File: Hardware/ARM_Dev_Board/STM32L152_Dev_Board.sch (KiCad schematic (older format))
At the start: 21 parts, among them J1 SWD_Header, J2 Conn_01x20_Female, J3 Conn_01x22_Female, J4 Eurorack_10_pin_power, SW1 SW_Push, U1 STM32L451CCUx, U4 LM1117-3.3, Y1 Crystal

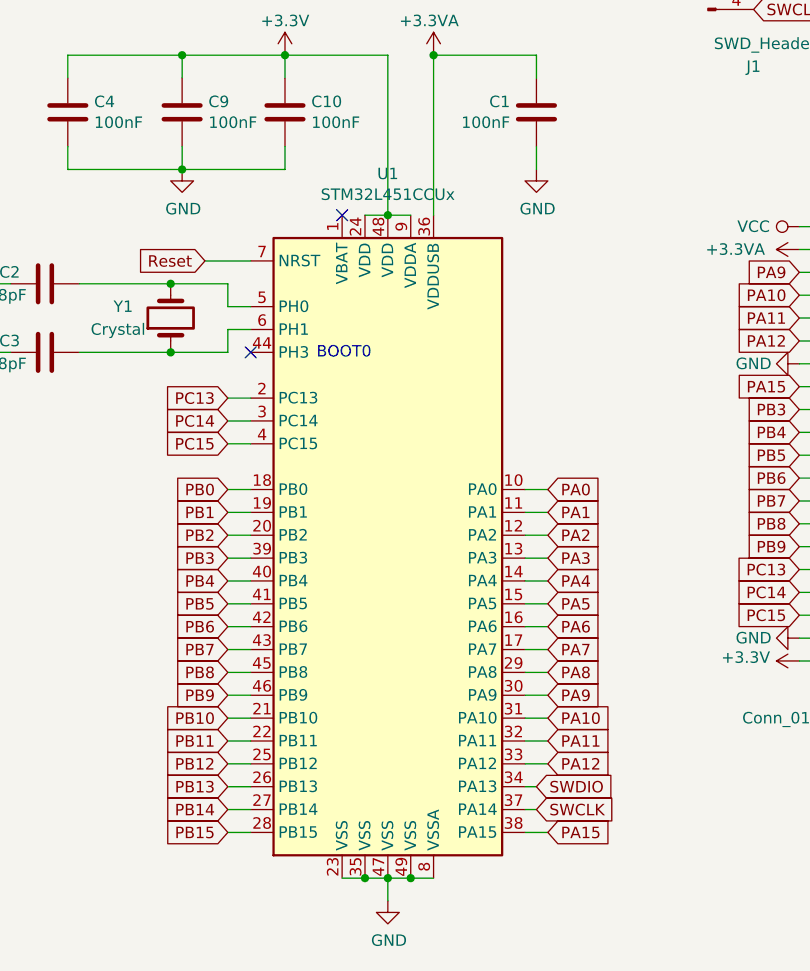
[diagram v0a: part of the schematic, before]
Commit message: Dev Board 1.1 layout finalised and gerbers sent to manufacturing
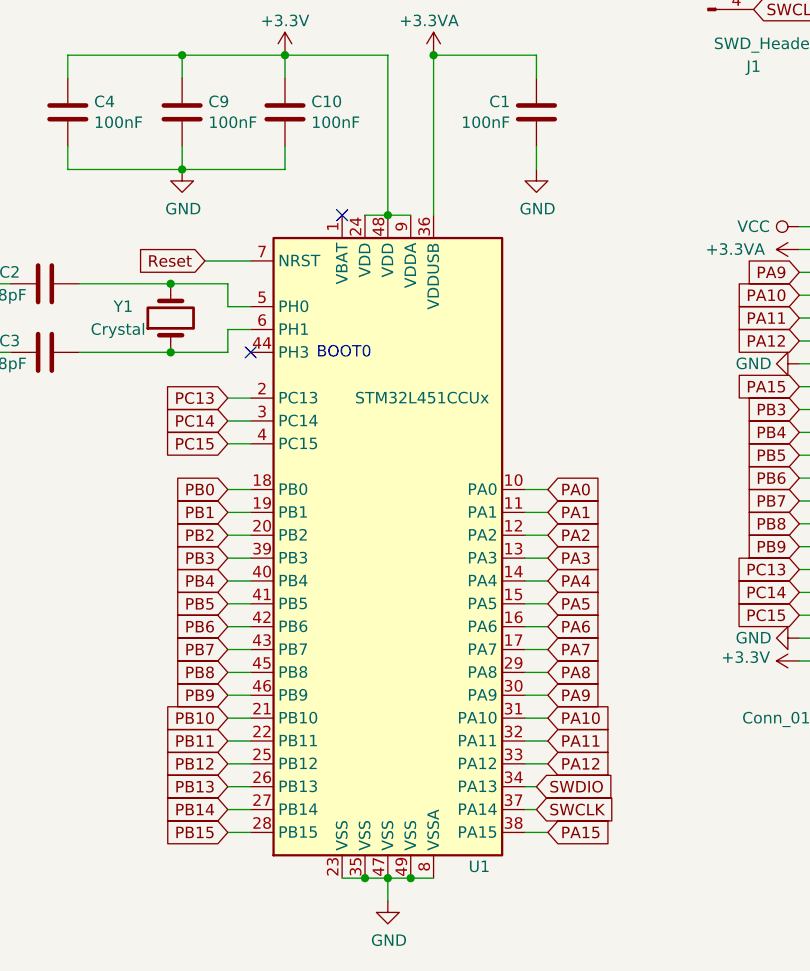
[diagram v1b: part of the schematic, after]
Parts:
- U4: footprint TO_SOT_Packages_SMD:TO-252-3_TabPin2 -> TO_SOT_Packages_SMD:SOT-223
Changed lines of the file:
@@
 F 0 "U4" H 7600 3892 50  0000 C CNN
 F 1 "LM1117-3.3" H 7600 3801 50  0000 C CNN
-F 2 "TO_SOT_Packages_SMD:TO-252-3_TabPin2" H 7600 3650 50  0001 C CNN
+F 2 "TO_SOT_Packages_SMD:SOT-223" H 7600 3650 50  0001 C CNN
 F 3 "http://www.ti.com/lit/ds/symlink/lm1117.pdf" H 7600 3650 50  0001 C CNN
 	1    7600 3650
@@
 U 1 1 5E448758
 P 2550 3750
-F 0 "U1" H 2550 5331 50  0000 C CNN
-F 1 "STM32L451CCUx" H 2550 5240 50  0000 C CNN
+F 0 "U1" H 2950 2300 50  0000 C CNN
+F 1 "STM32L451CCUx" H 2700 4350 50  0000 C CNN
 F 2 "Custom_Footprints:ARM-UQFN-48-7x7mm_Pitch0.5mm" H 2050 2350 50  0001 R CNN
 F 3 "http://www.st.com/st-web-ui/static/active/en/resource/technical/document/datasheet/DM00340475.pdf" H 2550 3750 50  0001 C CNN
@@
 $EndComp
 $Comp
-L power:+3.3VA #PWR?
+L power:+3.3VA #PWR0113
 U 1 1 5E98768A
 P 4350 2500
-F 0 "#PWR?" H 4350 2350 50  0001 C CNN
+F 0 "#PWR0113" H 4350 2350 50  0001 C CNN
 F 1 "+3.3VA" V 4350 2650 50  0000 L CNN
 F 2 "" H 4350 2500 50  0001 C CNN

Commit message: Added early draft of support for ICE40UP5k FPGA
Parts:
- C22, C23: footprint Capacitors_SMD:CP_Elec_4x5.8 -> Custom_Footprints:CP_Elec_4x5.8_Big_pad
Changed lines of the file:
@@
 F 0 "C22" V 7395 1450 50  0000 C CNN
 F 1 "22uF" V 7486 1450 50  0000 C CNN
-F 2 "Capacitors_SMD:CP_Elec_4x5.8" H 7688 1300 50  0001 C CNN
+F 2 "Custom_Footprints:CP_Elec_4x5.8_Big_pad" H 7688 1300 50  0001 C CNN
 F 3 "~" H 7650 1450 50  0001 C CNN
 	1    7650 1450
@@
 F 0 "C23" V 7905 2800 50  0000 C CNN
 F 1 "22uF" V 7814 2800 50  0000 C CNN
-F 2 "Capacitors_SMD:CP_Elec_4x5.8" H 7688 2650 50  0001 C CNN
+F 2 "Custom_Footprints:CP_Elec_4x5.8_Big_pad" H 7688 2650 50  0001 C CNN
 F 3 "~" H 7650 2800 50  0001 C CNN
 	1    7650 2800

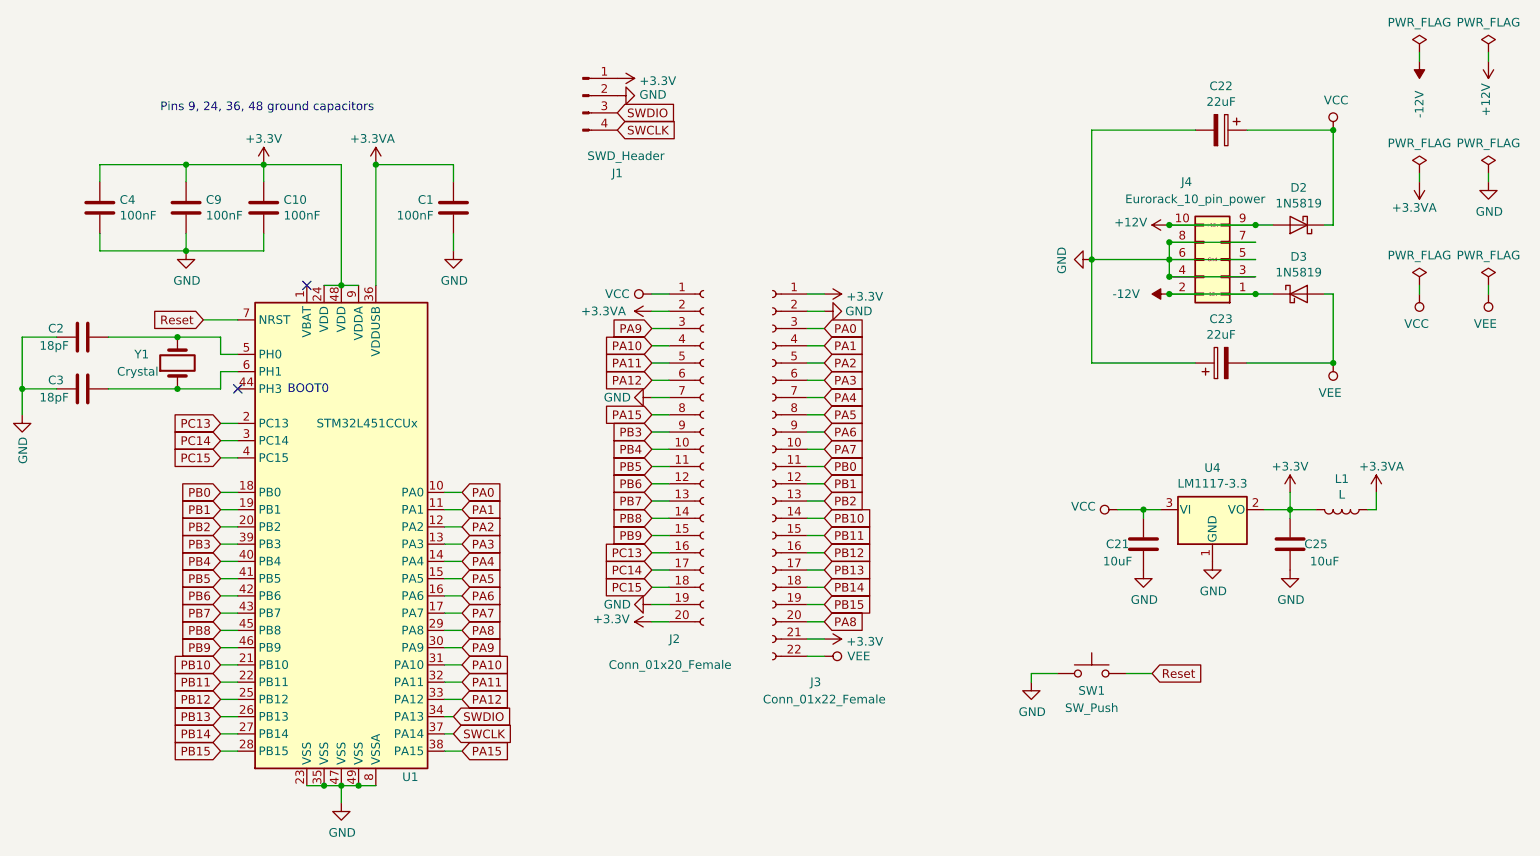
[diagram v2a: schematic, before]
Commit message: Rev 2 of dev board; provisional handling for overflow on output samples
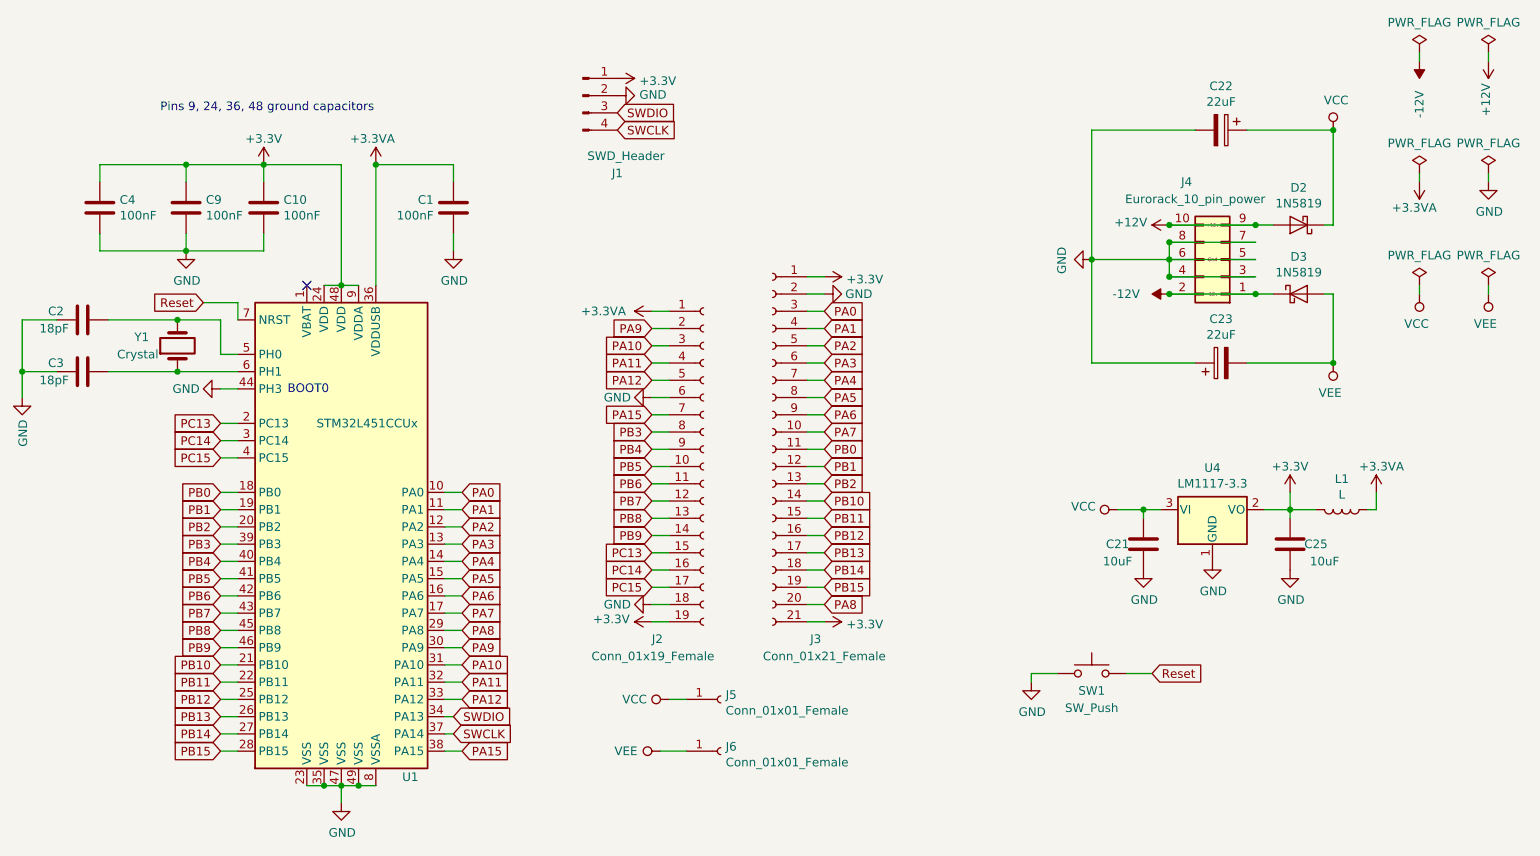
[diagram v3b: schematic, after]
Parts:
- removed J2: Conn_01x20_Female, Pin_Headers:Pin_Header_Straight_1x20_Pitch2.54mm, symbol Connector:Conn_01x20_Female
- removed J3: Conn_01x22_Female, Pin_Headers:Pin_Header_Straight_1x22_Pitch2.54mm, symbol Connector:Conn_01x22_Female
- added J2: Conn_01x19_Female, Pin_Headers:Pin_Header_Straight_1x19_Pitch2.54mm, symbol Connector:Conn_01x19_Female
- added J3: Conn_01x21_Female, Pin_Headers:Pin_Header_Straight_1x21_Pitch2.54mm, symbol Connector:Conn_01x21_Female
- added J5, J6: Conn_01x01_Female, Pin_Headers:Pin_Header_Straight_1x01_Pitch2.54mm, symbol Connector:Conn_01x01_Female
- Y1: footprint Custom_Footprints:Crystal_SMD -> Crystals:Crystal_SMD_0603-2pin_6.0x3.5mm_HandSoldering
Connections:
- net +3.3VA: now also J2.1 (Pin_1)
- net +3V3: now also J2.19 (Pin_19), J3.1 (Pin_1), J3.21 (Pin_21)
- net GND: now also U1.44 (PH3), J2.18 (Pin_18), J2.6 (Pin_6), J3.2 (Pin_2)
- net PA0: now also J3.3 (Pin_3)
- net PA1: now also J3.4 (Pin_4)
- net PA10: now also J2.3 (Pin_3)
- net PA11: now also J2.4 (Pin_4)
- net PA12: now also J2.5 (Pin_5)
- net PA15: now also J2.7 (Pin_7)
- net PA2: now also J3.5 (Pin_5)
- net PA3: now also J3.6 (Pin_6)
- net PA4: now also J3.7 (Pin_7)
- net PA5: now also J3.8 (Pin_8)
- net PA6: now also J3.9 (Pin_9)
- net PA7: now also J3.10 (Pin_10)
- net PA8: now also J3.20 (Pin_20)
- net PA9: now also J2.2 (Pin_2)
- net PB0: now also J3.11 (Pin_11)
- net PB1: now also J3.12 (Pin_12)
- net PB10: now also J3.14 (Pin_14)
- net PB11: now also J3.15 (Pin_15)
- net PB12: now also J3.16 (Pin_16)
- net PB13: now also J3.17 (Pin_17)
- net PB14: now also J3.18 (Pin_18)
- net PB15: now also J3.19 (Pin_19)
- net PB2: now also J3.13 (Pin_13)
- net PB3: now also J2.8 (Pin_8)
- net PB4: now also J2.9 (Pin_9)
- net PB5: now also J2.10 (Pin_10)
- net PB6: now also J2.11 (Pin_11)
- net PB7: now also J2.12 (Pin_12)
- net PB8: now also J2.13 (Pin_13)
- net PB9: now also J2.14 (Pin_14)
- net PC13: now also J2.15 (Pin_15)
- net PC14: now also J2.16 (Pin_16)
- net PC15: now also J2.17 (Pin_17)
- net VCC: now also J5.1 (Pin_1)
- net VEE: now also J6.1 (Pin_1)
- no-connect marks 2 -> 1
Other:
- moved on the sheet: C2, C3, Y1

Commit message: Fixes to schematic (missing resistor on 1.2V LDO); Created new implementation to support production board; added FPGA tester project
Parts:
- U1: footprint Custom_Footprints:ARM-UQFN-48-7x7mm_Pitch0.5mm -> Custom_Footprints:ICE40_QFN-48-1EP_7x7mm_Pitch0.5mm
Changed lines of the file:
@@
 F 0 "U1" H 2950 2300 50  0000 C CNN
 F 1 "STM32L451CCUx" H 2700 4350 50  0000 C CNN
-F 2 "Custom_Footprints:ARM-UQFN-48-7x7mm_Pitch0.5mm" H 2050 2350 50  0001 R CNN
+F 2 "Custom_Footprints:ICE40_QFN-48-1EP_7x7mm_Pitch0.5mm" H 2050 2350 50  0001 R CNN
 F 3 "http://www.st.com/st-web-ui/static/active/en/resource/technical/document/datasheet/DM00340475.pdf" H 2550 3750 50  0001 C CNN
 	1    2550 3750
